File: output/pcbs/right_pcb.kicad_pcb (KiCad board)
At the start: 2 copper layers, 161.7 x 89.3 mm, 54 parts

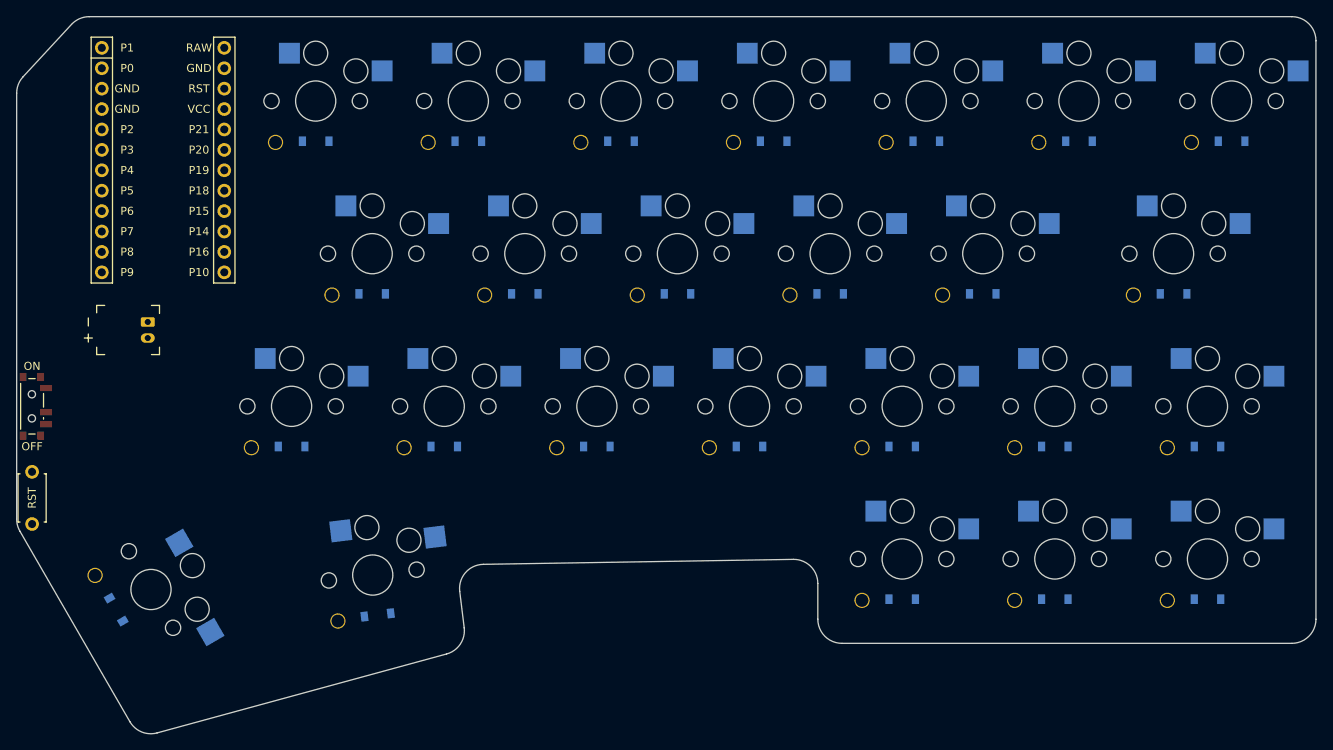
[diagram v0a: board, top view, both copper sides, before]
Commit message: right side mx switches and row and column nets
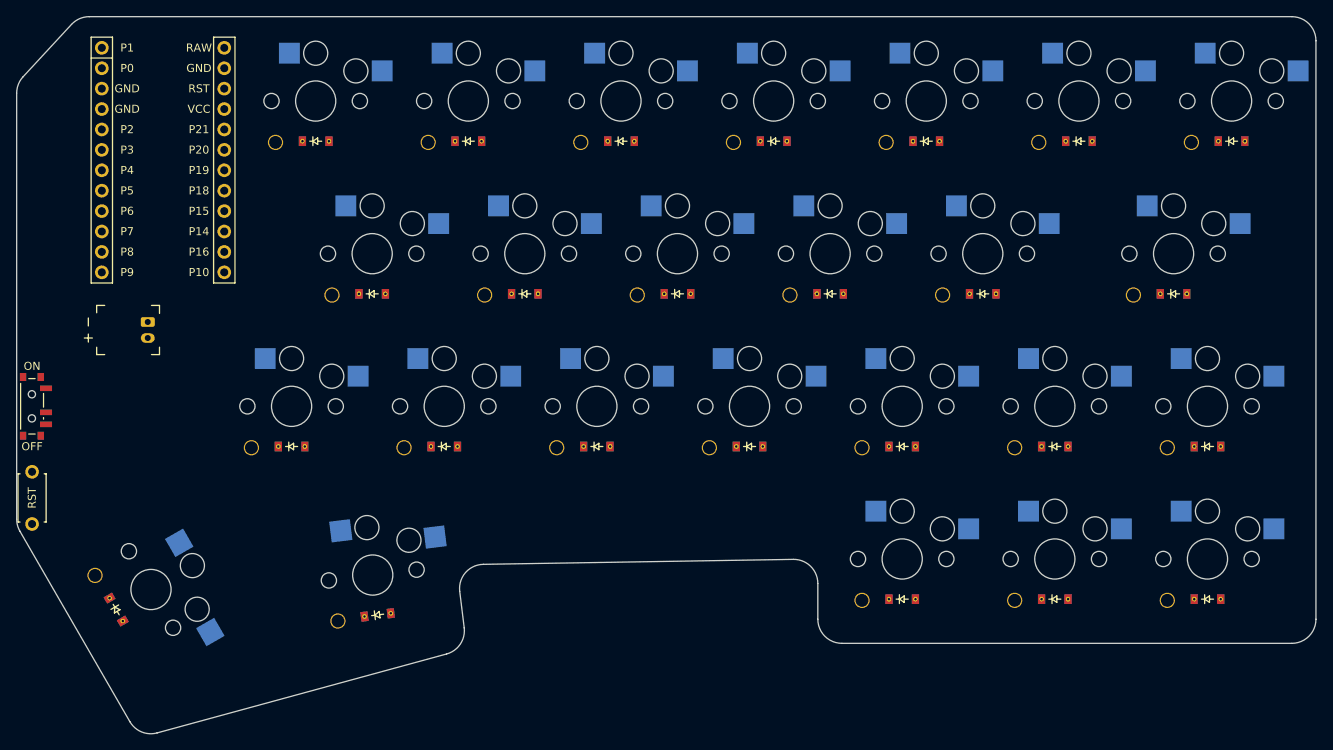
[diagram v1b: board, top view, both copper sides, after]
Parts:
- D1, D10, D11, D12, D13, D14, D15, D16, D17, D18, D19, D2, D20, D21, D22, D23, D24, D25, D3, D4, D5, D6, D7, D8, D9: footprint ceoloide:diode_tht_sod123 -> ComboDiode; moved to F.Cu
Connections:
- D1 pad 1: (no net) -> y_single
- D10 pad 1: (no net) -> k_single
- D11 pad 1: (no net) -> l_single
- D12 pad 1: (no net) -> colon_single
- D13 pad 1: (no net) -> quotes_single
- D14 pad 1: (no net) -> b_single
- D15 pad 1: (no net) -> n_single
- D16 pad 1: (no net) -> m_single
- D17 pad 1: (no net) -> comma_single
- D18 pad 1: (no net) -> peroid_single
- D19 pad 1: (no net) -> up_arrow_single
- D2 pad 1: (no net) -> u_single
- D20 pad 1: (no net) -> slash_single
- D21 pad 1: (no net) -> larrow_single
- D22 pad 1: (no net) -> darrow_single
- D23 pad 1: (no net) -> rarrow_single
- D24 pad 1: (no net) -> space_single
- D25 pad 1: (no net) -> raise_single
- D3 pad 1: (no net) -> i_single
- D4 pad 1: (no net) -> o_single
- D5 pad 1: (no net) -> p_single
- D6 pad 1: (no net) -> backspace_single
- D7 pad 1: (no net) -> delete_single
- D8 pad 1: (no net) -> h_single
- D9 pad 1: (no net) -> j_single
- S1 pad 1: (no net) -> P0
- S10 pad 1: (no net) -> P2
- S11 pad 1: (no net) -> P3
- S12 pad 1: (no net) -> P4
- S13 pad 1: (no net) -> P5
- S14 pad 1: (no net) -> P0
- S15 pad 1: (no net) -> P1
- S16 pad 1: (no net) -> P2
- S17 pad 1: (no net) -> P3
- S18 pad 1: (no net) -> P4
- S19 pad 1: (no net) -> P5
- S2 pad 1: (no net) -> P1
- S20 pad 1: (no net) -> P6
- S21 pad 1: (no net) -> P4
- S22 pad 1: (no net) -> P5
- S23 pad 1: (no net) -> P6
- S24 pad 1: (no net) -> P0
- S25 pad 1: (no net) -> P1
- S3 pad 1: (no net) -> P2
- S4 pad 1: (no net) -> P3
- S5 pad 1: (no net) -> P4
- S6 pad 1: (no net) -> P5
- S7 pad 1: (no net) -> P6
- S8 pad 1: (no net) -> P0
- S9 pad 1: (no net) -> P1

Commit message: right side changes like mx switch
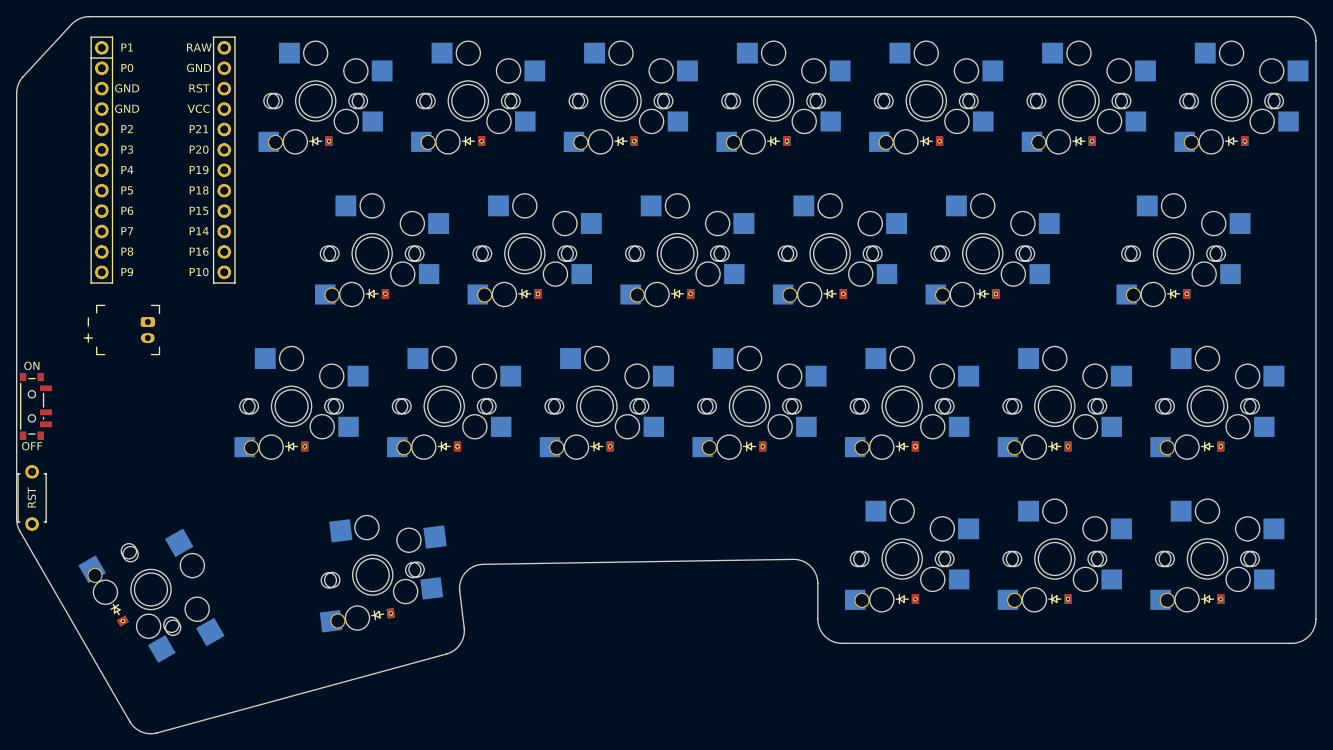
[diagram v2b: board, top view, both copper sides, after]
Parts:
- added S26: , ceoloide:switch_mx, B.Cu at (150.0, 100.0)
- added S27: , ceoloide:switch_mx, B.Cu at (169.0, 100.0)
- added S28: , ceoloide:switch_mx, B.Cu at (188.0, 100.0)
- added S29: , ceoloide:switch_mx, B.Cu at (207.0, 100.0)
- added S30: , ceoloide:switch_mx, B.Cu at (226.0, 100.0)
- added S31: , ceoloide:switch_mx, B.Cu at (245.0, 100.0)
- added S32: , ceoloide:switch_mx, B.Cu at (264.0, 100.0)
- added S33: , ceoloide:switch_mx, B.Cu at (157.0, 119.0)
- added S34: , ceoloide:switch_mx, B.Cu at (176.0, 119.0)
- added S35: , ceoloide:switch_mx, B.Cu at (195.0, 119.0)
- added S36: , ceoloide:switch_mx, B.Cu at (214.0, 119.0)
- added S37: , ceoloide:switch_mx, B.Cu at (233.0, 119.0)
- added S38: , ceoloide:switch_mx, B.Cu at (256.8, 119.0)
- added S39: , ceoloide:switch_mx, B.Cu at (147.0, 138.0)
- added S40: , ceoloide:switch_mx, B.Cu at (166.0, 138.0)
- added S41: , ceoloide:switch_mx, B.Cu at (185.0, 138.0)
- added S42: , ceoloide:switch_mx, B.Cu at (204.0, 138.0)
- added S43: , ceoloide:switch_mx, B.Cu at (223.0, 138.0)
- added S44: , ceoloide:switch_mx, B.Cu at (242.0, 138.0)
- added S45: , ceoloide:switch_mx, B.Cu at (261.0, 138.0)
- added S46: , ceoloide:switch_mx, B.Cu at (223.0, 157.0)
- added S47: , ceoloide:switch_mx, B.Cu at (242.0, 157.0)
- added S48: , ceoloide:switch_mx, B.Cu at (261.0, 157.0)
- added S49: , ceoloide:switch_mx, B.Cu at (129.5, 160.8)
- added S50: , ceoloide:switch_mx, B.Cu at (157.1, 159.0)
